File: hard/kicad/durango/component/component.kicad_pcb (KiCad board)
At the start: 2 copper layers, 40 parts, among them J1 SCART, J2 Component Video [Pr/Pb/Y], J3 Audio, Q1 BC548, Q2 BC548, Q3 BC548, Q4 BC548

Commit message: preliminary RGB2YUV board
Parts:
- moved C3 183.0 mm to (63.5, 76.2), turned to 180 degrees
- moved C1 181.2 mm to (63.5, 61.0), turned to 180 degrees
- moved D1 181.1 mm to (69.8, 48.3)
- moved C7 180.1 mm to (67.3, 64.8), turned to 180 degrees
- moved C6 170.1 mm to (67.3, 72.4), turned to 180 degrees
- moved C2 170.1 mm to (63.5, 68.6), turned to 180 degrees
- moved C5 165.4 mm to (67.3, 80.0), turned to 180 degrees
- moved Q3 155.0 mm to (86.4, 77.5)
- moved R7 153.0 mm to (80.0, 68.6), turned to 180 degrees
- moved C4 149.1 mm to (100.3, 57.1)
- moved C9 146.9 mm to (78.7, 96.5), turned to 180 degrees
- moved R6 145.0 mm to (80.0, 61.0), turned to 180 degrees
- moved Q4 144.2 mm to (86.4, 72.4)
- moved Q2 142.5 mm to (86.4, 67.3)
- moved C8 141.4 mm to (100.3, 81.3)
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
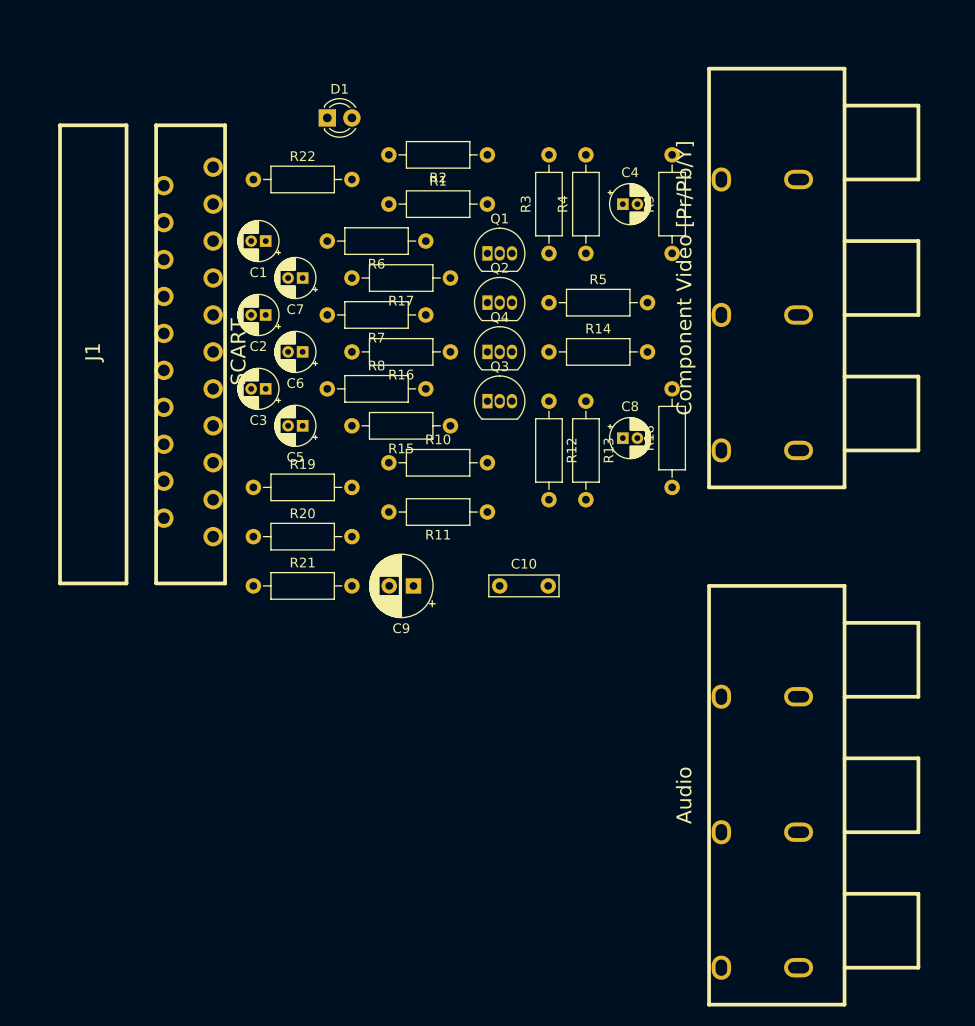
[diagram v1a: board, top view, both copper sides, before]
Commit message: almost definitive RGB to YUV converter
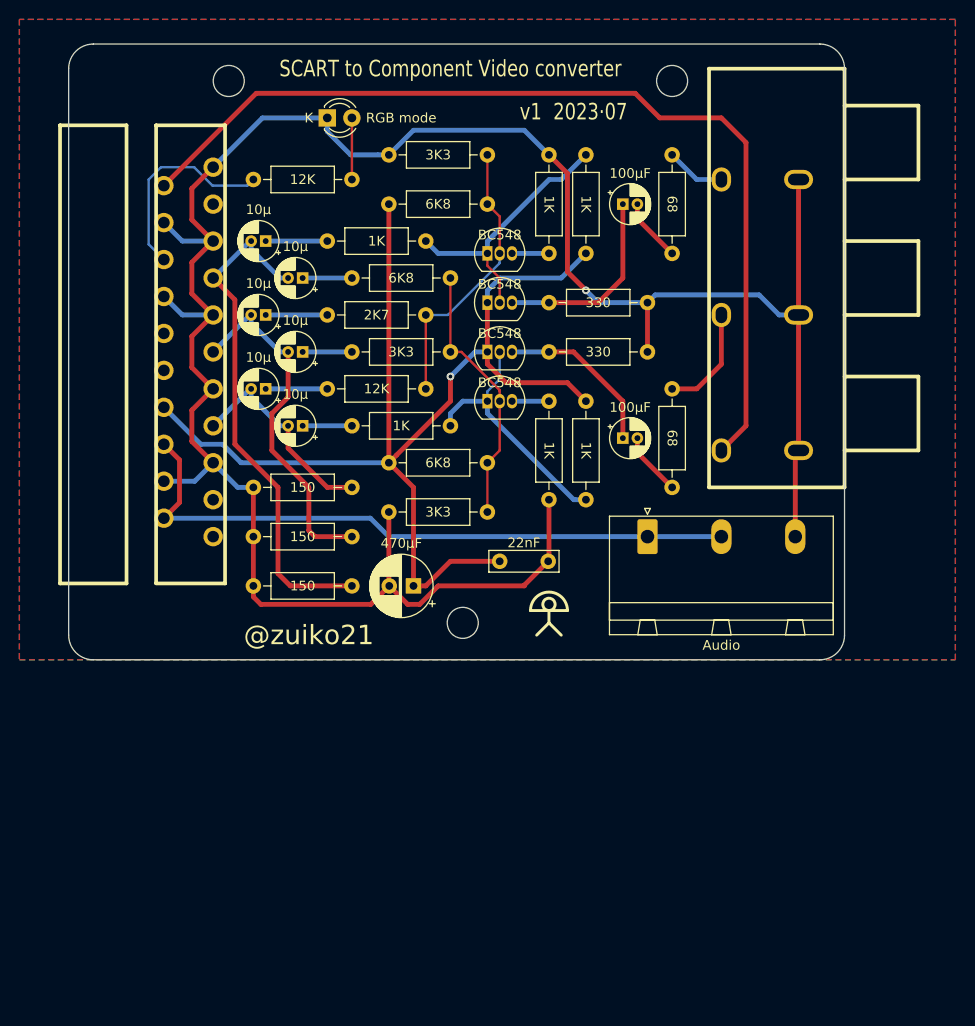
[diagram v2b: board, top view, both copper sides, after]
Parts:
- added H1: M3, MountingHole:MountingHole_3.2mm_M3_DIN965, F.Cu at (59.7, 44.5)
- added H2: M3, MountingHole:MountingHole_3.2mm_M3_DIN965, F.Cu at (105.4, 44.5)
- added H3: M3, MountingHole:MountingHole_3.2mm_M3_DIN965, F.Cu at (83.8, 100.3)
- added LOGO1: Logo_Open_Hardware_Small, durango:jaqueria, B.Cu at (95.2, 45.7)
- D1: value LED -> RGB mode
- J3: footprint durango:3xRCA -> Connector_Phoenix_GMSTB:PhoenixContact_GMSTBA_2,5_3-G-7,62_1x03_P7.62mm_Horizontal
- moved J3 35.3 mm to (102.9, 91.4), turned to 0 degrees
- moved R8 10.2 mm to (80.0, 76.2), turned to 180 degrees
- moved C10 2.54 mm to (87.6, 94.0)
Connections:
- J3 pad 2: GND -> /AUDIO
- J3 pad 3: /AUDIO -> GND
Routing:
- net GND: track 0.00 -> 242.7 mm, vias 0 -> 1
- net +5V: track 0.00 -> 123.4 mm, vias 0 -> 1
- net /Y: track 0.00 -> 98.9 mm
- net /AUDIO: track 0.00 -> 67.2 mm
- net /R: track 0.00 -> 52.8 mm
- net /G: track 0.00 -> 36.8 mm
- net /BIASr: track 0.00 -> 29.1 mm
- net /UR: track 0.00 -> 27.6 mm
- net /BIASb: track 0.00 -> 27.4 mm
- net /UB: track 0.00 -> 26.3 mm
- net /B: track 0.00 -> 21.9 mm
- net /RGB: track 0.00 -> 21.3 mm
- net /BUFr: track 0.00 -> 20.1 mm
- net /BUFb: track 0.00 -> 17.3 mm
- net /Pb: track 0.00 -> 11.2 mm
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- added copper zone on B.Cu, net +5V
- added copper zone on F.Cu, net GND
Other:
- board outline added: 80 x 63.5 mm
- board text added: "@zuiko21"
- board text added: "K"
- board text added: "SCART to Component Video converter"
- board text added: "v1 2023·07"

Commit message: put 2xRCA footprint on RGB2YUV
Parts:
- J2: value Component Video [Pr/Pb/Y] -> Component Video [Y/Pb/Pr]
- J3: footprint Connector_Phoenix_GMSTB:PhoenixContact_GMSTBA_2,5_3-G-7,62_1x03_P7.62mm_Horizontal -> durango:2xRCA_vertical
- moved J3 22.2 mm to (123.2, 100.3), turned to 90 degrees
- moved LOGO1 6.98 mm to (88.3, 45.7)
- moved C8 1.27 mm to (100.3, 82.5)
- moved J2 1.27 mm to (120.7, 67.3)
- moved R18 1.27 mm to (105.4, 87.6)
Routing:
- net GND: track 242.7 -> 250.5 mm
- net /AUDIO: track 67.2 -> 75.0 mm
- net /Pb: track 11.2 -> 13.8 mm
- net /Y: track 98.9 -> 97.6 mm
- net /BUFb: track 17.3 -> 18.6 mm
- net /Pr: track 6.13 -> 5.61 mm
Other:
- board text added: "Pb"
- board text added: "Pr"
- board text added: "Y"
- board text added: "for Durango·X"

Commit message: ready for plotting
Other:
- board text added: "JLCJLCJLCJLC"
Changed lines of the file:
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@@
   (general
     (thickness 1.6)
-    (drawings 22)
+    (drawings 23)
     (tracks 196)
     (zones 0)
@@
   )
   (setup
-    (last_trace_width 0.5)
+    (last_trace_width 0.25)
     (user_trace_width 0.5)
     (trace_clearance 0.2)
@@
     (pcbplotparams
       (layerselection 0x010fc_ffffffff)
-      (usegerberextensions false)
+      (usegerberextensions true)
       (usegerberattributes false)
       (usegerberadvancedattributes false)
@@
       (plotinvisibletext false)
       (padsonsilk false)
-      (subtractmaskfromsilk false)
+      (subtractmaskfromsilk true)
       (outputformat 1)
       (mirror false)
-      (drillshape 1)
+      (drillshape 0)
       (scaleselection 1)
       (outputdirectory ""))
@@
     )
   )
+  (gr_text JLCJLCJLCJLC (at 99.06 97.79) (layer B.SilkS)
+    (effects (font (size 1 1) (thickness 0.15)) (justify mirror))
+  )
   (gr_text Y (at 107.95 81.28) (layer F.SilkS)

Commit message: revised RCA footprint and Component silkscreen
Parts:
- R18, R9: value 68 -> 75
- R19, R21: value 150 -> 120
- R20: value 150 -> 180
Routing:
- net GND: track 250.5 -> 243.0 mm
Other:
- board text added: "v1.1 2023·08"
- board text removed: "v1 2023·07"
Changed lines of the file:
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@@
   )
   (setup
-    (last_trace_width 0.25)
+    (last_trace_width 0.5)
     (user_trace_width 0.5)
     (trace_clearance 0.2)
@@
       (effects (font (size 1.524 1.524) (thickness 0.3048)) (justify mirror))
     )
-    (fp_text value Audio (at 5.08 -15.6972 270 unlocked) (layer F.SilkS)
+    (fp_text value Audio (at 5.08 -15.6972 270) (layer F.SilkS)
       (effects (font (size 1.524 1.524) (thickness 0.3048)))
     )
@@
     (pad 2 thru_hole circle (at 8.83 -12.5 90) (size 2 2) (drill 1.3) (layers *.Cu *.Mask)
       (net 19 /AUDIO))
-    (pad 3 thru_hole circle (at 1.33 -5.25 90) (size 2.2 2.2) (drill 1.5) (layers *.Cu *.Mask)
+    (pad 3 thru_hole circle (at 8.83 -5.25 90) (size 2.2 2.2) (drill 1.5) (layers *.Cu *.Mask)
       (net 14 GND))
     (model walter/conn_av/scart.wrl
@@
       (effects (font (size 1 1) (thickness 0.15)) (justify mirror))
     )
-    (fp_text value 150 (at 5.08 0) (layer F.SilkS)
+    (fp_text value 120 (at 5.08 0) (layer F.SilkS)
       (effects (font (size 1 1) (thickness 0.15)))
     )
@@
       (effects (font (size 1 1) (thickness 0.15)) (justify mirror))
     )
-    (fp_text value 150 (at 5.08 0) (layer F.SilkS)
+    (fp_text value 180 (at 5.08 0) (layer F.SilkS)
       (effects (font (size 1 1) (thickness 0.15)))
     )
@@
       (effects (font (size 1 1) (thickness 0.15)) (justify mirror))
     )
-    (fp_text value 150 (at 5.08 0) (layer F.SilkS)
+    (fp_text value 120 (at 5.08 0) (layer F.SilkS)
       (effects (font (size 1 1) (thickness 0.15)))
     )
@@
       (effects (font (size 1 1) (thickness 0.15)) (justify mirror))
     )
-    (fp_text value 68 (at 5.08 0 270 unlocked) (layer F.SilkS)
+    (fp_text value 75 (at 5.08 0 270 unlocked) (layer F.SilkS)
       (effects (font (size 1 1) (thickness 0.15)))
     )
@@
       (effects (font (size 1 1) (thickness 0.15)) (justify mirror))
     )
-    (fp_text value 68 (at 5.08 0 270 unlocked) (layer F.SilkS)
+    (fp_text value 75 (at 5.08 0 270 unlocked) (layer F.SilkS)
       (effects (font (size 1 1) (thickness 0.15)))
     )
@@
       (effects (font (size 1 1) (thickness 0.15)) (justify mirror))
     )
-    (fp_text value BC548 (at 1.27 -1.905) (layer F.SilkS)
+    (fp_text value BC548 (at -2.286 -0.254 270 unlocked) (layer F.SilkS)
       (effects (font (size 1 1) (thickness 0.15)))
     )
@@
       (effects (font (size 1 1) (thickness 0.15)) (justify mirror))
     )
-    (fp_text value BC548 (at 1.27 -1.905) (layer F.SilkS)
+    (fp_text value BC548 (at -2.286 0 270 unlocked) (layer F.SilkS)
       (effects (font (size 1 1) (thickness 0.15)))
     )
@@
       (effects (font (size 1 1) (thickness 0.15)) (justify mirror))
     )
-    (fp_text value BC548 (at 1.27 -1.905) (layer F.SilkS)
+    (fp_text value BC548 (at -2.286 -0.508 270 unlocked) (layer F.SilkS)
       (effects (font (size 1 1) (thickness 0.15)))
     )
@@
       (effects (font (size 1 1) (thickness 0.15)) (justify mirror))
     )
-    (fp_text value BC548 (at 1.27 -1.905) (layer F.SilkS)
+    (fp_text value BC548 (at -2.286 -0.762 270 unlocked) (layer F.SilkS)
       (effects (font (size 1 1) (thickness 0.15)))
     )
@@
     (effects (font (size 2 2) (thickness 0.4)))
   )
-  (gr_text "v1  2023·07" (at 95.25 47.625) (layer F.SilkS)
+  (gr_text "v1.1  2023·08" (at 94.615 47.625) (layer F.SilkS)
     (effects (font (size 1.7 1.35) (thickness 0.15)))
   )
@@
   (segment (start 90.17 96.52) (end 90.17 96.44) (width 0.5) (layer F.Cu) (net 14))
   (segment (start 118.45036 81.28) (end 118.45036 54.61) (width 0.5) (layer F.Cu) (net 14))
-  (segment (start 118.45036 98.48964) (end 117.94 99) (width 0.25) (layer F.Cu) (net 14))
-  (segment (start 118.45036 81.28) (end 118.45036 98.48964) (width 0.5) (layer F.Cu) (net 14))
   (segment (start 116.45087 67.31) (end 118.45036 67.31) (width 0.5) (layer B.Cu) (net 14))
   (segment (start 114.75137 65.6105) (end 116.45087 67.31) (width 0.5) (layer B.Cu) (net 14))
   (segment (start 104.5695 65.6105) (end 114.75137 65.6105) (width 0.5) (layer B.Cu) (net 14))
   (segment (start 102.87 67.31) (end 104.5695 65.6105) (width 0.5) (layer B.Cu) (net 14))
+  (segment (start 118.45036 90.98964) (end 117.94 91.5) (width 0.5) (layer F.Cu) (net 14))
+  (segment (start 118.45036 81.28) (end 118.45036 90.98964) (width 0.5) (layer F.Cu) (net 14))
   (segment (start 96.52 62.23) (end 93.98 64.77) (width 0.5) (layer B.Cu) (net 15))
   (segment (start 86.36 66.06) (end 86.36 67.31) (width 0.5) (layer B.Cu) (net 15))
